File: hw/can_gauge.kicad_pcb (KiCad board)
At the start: 2 copper layers, 28 parts, among them J1 Gauge 1, J2 Gauge 2, J3 Gauge 3, J4 Gauge 4, J5 Gauge 5, J6 Gauge 6, J7 Power & CAN, U1 PIC16F1459-IP, U4 74HC595, U5 74HC595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

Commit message: hw: data traces
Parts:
- moved U1 6.29 mm to (88.9, 79.5)
- moved C9 4.00 mm to (86.0, 73.5)
- moved C4 3.93 mm to (90.0, 73.5), turned to -90 degrees
- moved U6 1.00 mm to (75.5, 73.8)
- moved C8 0.50 mm to (78.0, 95.0)
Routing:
- net Net-(U1-PWM1/CWG1A/T0CKI/RC5): track 26.2 -> 93.4 mm
- net +5V: track 75.7 -> 142.3 mm
- net Net-(U1-CWG1B/C1OUT/C2OUT/RC4): track 25.2 -> 77.0 mm
- net Net-(U4-QH'): track 0.00 -> 41.8 mm
- net Net-(U1-CLKR/C1IN3-/C2IN3-/DACOUT2/AN7/RC3): track 0.00 -> 35.9 mm
- net Net-(U5-QH'): track 39.6 -> 42.7 mm
- net Net-(U6-QG): track 14.3 -> 14.8 mm
- net GND: track 0.50 -> 0.00 mm, vias 20 -> 22

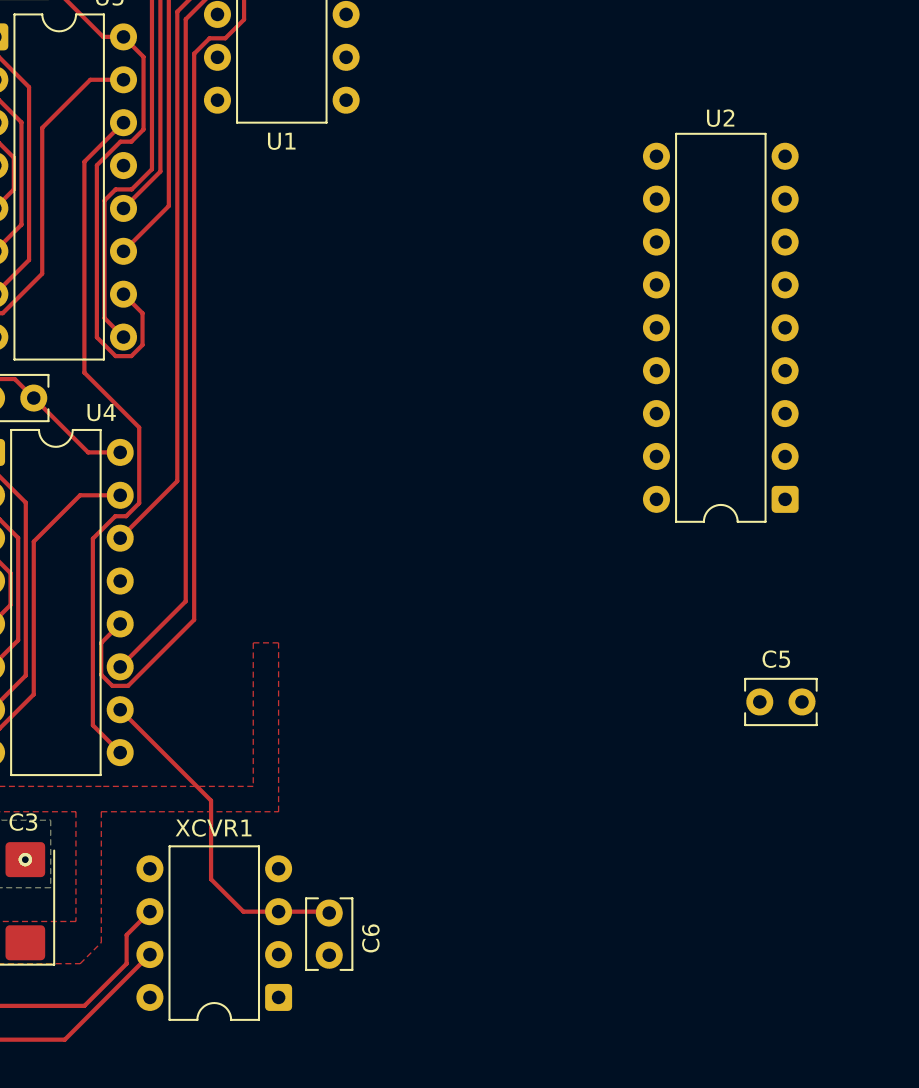
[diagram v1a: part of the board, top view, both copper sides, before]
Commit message: hw: rx,tx traces
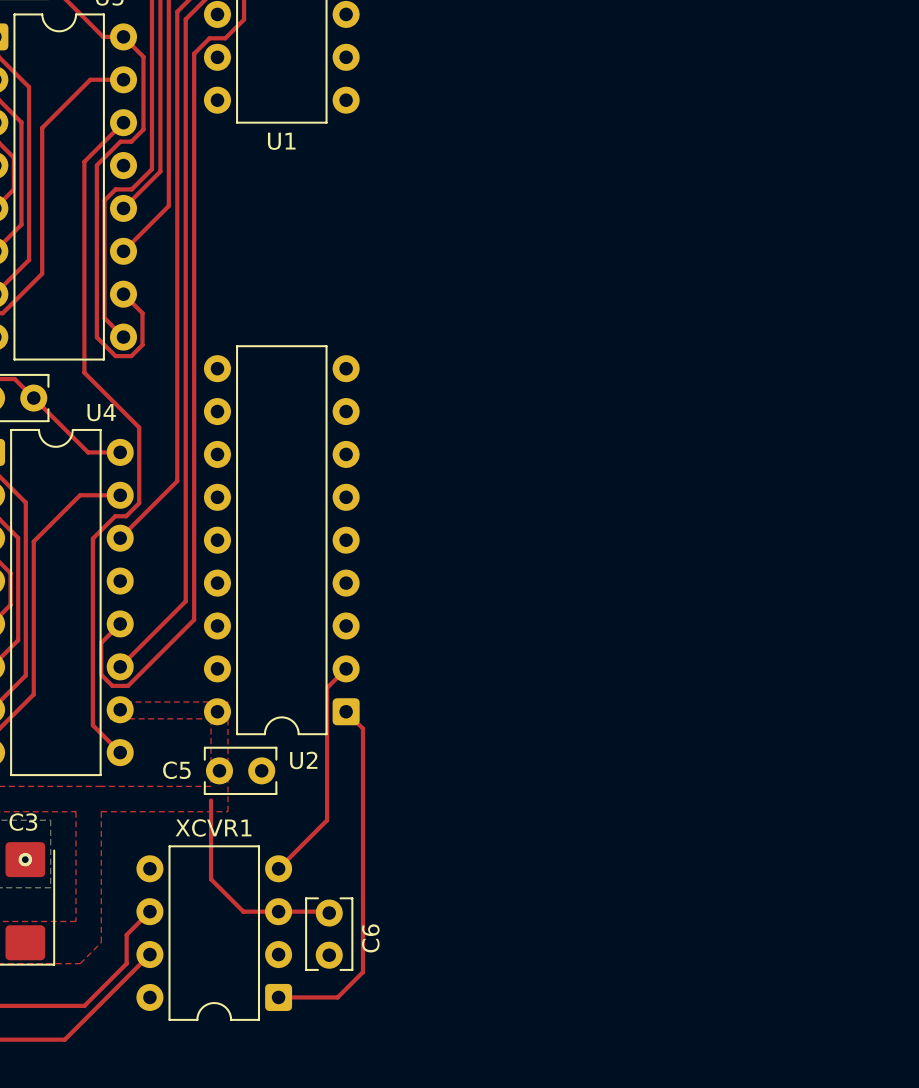
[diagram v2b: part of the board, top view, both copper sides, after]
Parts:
- moved C5 34.7 mm to (89.0, 142.1), turned to 0 degrees
- moved U2 28.9 mm to (96.5, 138.6)
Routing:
- net TX: track 0.27 -> 21.5 mm
- net RX: track 0.00 -> 13.5 mm
- net +5V: track 142.3 -> 134.7 mm
- net GND: vias 22 -> 23
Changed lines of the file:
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@@
 	(footprint "Capacitor_THT:C_Rect_L4.0mm_W2.5mm_P2.50mm"
 		(layer "F.Cu")
-		(at 123.5 138 180)
+		(at 89 142.08)
 		(descr "C, Rect series, Radial, pin pitch=2.50mm, , length*width=4*2.5mm^2, Capacitor")
 		(tags "C Rect series Radial pin pitch 2.50mm  length 4mm width 2.5mm Capacitor")
 		(property "Reference" "C5"
-			(at 1.5 2.5 0)
+			(at -2.5 0 0)
 			(layer "F.SilkS")
 			(effects
@@
 		)
 		(property "Datasheet" "https://product.tdk.com/en/system/files/dam/doc/product/capacitor/ceramic/lead-mlcc/catalog/leadmlcc_halogenfree_fa_en.pdf"
-			(at 0 0 180)
+			(at 0 0 0)
 			(unlocked yes)
 			(layer "F.Fab")
@@
 		)
 		(property "Description" "Unpolarized capacitor, small symbol"
-			(at 0 0 180)
+			(at 0 0 0)
 			(unlocked yes)
 			(layer "F.Fab")
@@
 		)
 		(property "Digikey" "https://www.digikey.ca/en/products/detail/tdk-corporation/FA18X7R1H104KNU06/5863626"
-			(at 0 0 180)
+			(at 0 0 0)
 			(unlocked yes)
 			(layer "F.Fab")
@@
 		(attr through_hole)
 		(fp_line
-			(start 3.37 0.665)
-			(end 3.37 1.37)
+			(start -0.87 -1.37)
+			(end -0.87 -0.665)
 			(stroke
 				(width 0.12)
@@
 		)
 		(fp_line
-			(start 3.37 -1.37)
-			(end 3.37 -0.665)
+			(start -0.87 -1.37)
+			(end 3.37 -1.37)
 			(stroke
 				(width 0.12)
@@
 		)
 		(fp_line
-			(start -0.87 1.37)
-			(end 3.37 1.37)
+			(start -0.87 0.665)
+			(end -0.87 1.37)
 			(stroke
 				(width 0.12)
@@
 		)
 		(fp_line
-			(start -0.87 0.665)
-			(end -0.87 1.37)
+			(start -0.87 1.37)
+			(end 3.37 1.37)
 			(stroke
 				(width 0.12)
@@
 		)
 		(fp_line
-			(start -0.87 -1.37)
-			(end 3.37 -1.37)
+			(start 3.37 -1.37)
+			(end 3.37 -0.665)
 			(stroke
 				(width 0.12)
@@
 		)
 		(fp_line
-			(start -0.87 -1.37)
-			(end -0.87 -0.665)
+			(start 3.37 0.665)
+			(end 3.37 1.37)
 			(stroke
 				(width 0.12)
@@
 		)
 		(fp_line
-			(start 3.55 1.5)
-			(end 3.55 -1.5)
+			(start -1.05 -1.5)
+			(end -1.05 1.5)
 			(stroke
 				(width 0.05)
@@
 		)
 		(fp_line
-			(start 3.55 -1.5)
-			(end -1.05 -1.5)
+			(start -1.05 1.5)
+			(end 3.55 1.5)
 			(stroke
 				(width 0.05)
@@
 		)
 		(fp_line
-			(start -1.05 1.5)
-			(end 3.55 1.5)
+			(start 3.55 -1.5)
+			(end -1.05 -1.5)
 			(stroke
 				(width 0.05)
@@
 		)
 		(fp_line
-			(start -1.05 -1.5)
-			(end -1.05 1.5)
+			(start 3.55 1.5)
+			(end 3.55 -1.5)
 			(stroke
 				(width 0.05)
@@
 		)
 		(fp_line
-			(start 3.25 1.25)
-			(end 3.25 -1.25)
+			(start -0.75 -1.25)
+			(end -0.75 1.25)
 			(stroke
 				(width 0.1)
@@
 		)
 		(fp_line
-			(start 3.25 -1.25)
-			(end -0.75 -1.25)
+			(start -0.75 1.25)
+			(end 3.25 1.25)
 			(stroke
 				(width 0.1)
@@
 		)
 		(fp_line
-			(start -0.75 1.25)
-			(end 3.25 1.25)
+			(start 3.25 -1.25)
+			(end -0.75 -1.25)
 			(stroke
 				(width 0.1)
@@
 		)
 		(fp_line
-			(start -0.75 -1.25)
-			(end -0.75 1.25)
+			(start 3.25 1.25)
+			(end 3.25 -1.25)
 			(stroke
 				(width 0.1)
@@
 		)
 		(pad "1" thru_hole circle
-			(at 0 0 180)
+			(at 0 0)
 			(size 1.6 1.6)
 			(drill 0.8)
@@
 		)
 		(pad "2" thru_hole circle
-			(at 2.5 0 180)
+			(at 2.5 0)
 			(size 1.6 1.6)
 			(drill 0.8)
@@
 	(footprint "Package_DIP:DIP-18_W7.62mm"
 		(layer "F.Cu")
-		(at 122.5 126 180)
+		(at 96.5 138.58 180)
 		(descr "18-lead though-hole mounted DIP package, row spacing 7.62mm (300 mils)")
 		(tags "THT DIP DIL PDIP 2.54mm 7.62mm 300mil")
 		(property "Reference" "U2"
-			(at 3.81 22.54 0)
+			(at 2.5 -2.92 0)
 			(layer "F.SilkS")
 			(effects
@@
 	)
 	(via
+		(at 91.5 142.08)
+		(size 0.8)
+		(drill 0.4)
+		(layers "F.Cu" "B.Cu")
+		(net 1)
+	)
+	(via
 		(at 71.62 120.8)
 		(size 0.8)
@@
 	)
 	(via
-		(at 122.5 105.68)
+		(at 96.5 118.26)
 		(size 0.8)
 		(drill 0.4)
@@
 	)
 	(segment
-		(start 83.12 138.46)
-		(end 88.5 143.84)
-		(width 0.25)
-		(layer "F.Cu")
-		(net 3)
-	)
-	(segment
 		(start 88 73.5)
 		(end 90 73.5)
@@
 	)
 	(segment
-		(start 122.31 125.69)
-		(end 122.5 125.5)
+		(start 95.374 145.006)
+		(end 95.374 137.166)
+		(width 0.25)
+		(layer "F.Cu")
+		(net 50)
+	)
+	(segment
+		(start 95.374 137.166)
+		(end 96.5 136.04)
+		(width 0.25)
+		(layer "F.Cu")
+		(net 50)
+	)
+	(segment
+		(start 92.5 147.88)
+		(end 95.374 145.006)
+		(width 0.25)
+		(layer "F.Cu")
+		(net 50)
+	)
+	(segment
+		(start 97.5 139.58)
+		(end 96.5 138.58)
+		(width 0.25)
+		(layer "F.Cu")
+		(net 53)
+	)
+	(segment
+		(start 96 155.5)
+		(end 97.5 154)
+		(width 0.25)
+		(layer "F.Cu")
+		(net 53)
+	)
+	(segment
+		(start 92.5 155.5)
+		(end 96 155.5)
+		(width 0.25)
+		(layer "F.Cu")
+		(net 53)
+	)
+	(segment
+		(start 97.5 154)
+		(end 97.5 139.58)
 		(width 0.25)
 		(layer "F.Cu")
@@
 			(pts
 				(xy 67.5 143) (xy 67.5 142.5) (xy 66 142.5) (xy 66 144.5) (xy 80.5 144.5) (xy 80.5 151) (xy 68.5 151)
-				(xy 68.5 153.5) (xy 80.75 153.5) (xy 82 152.25) (xy 82 144.5) (xy 92.5 144.5) (xy 92.5 134.5) (xy 91 134.5)
-				(xy 91 143) (xy 82 143)
+				(xy 68.5 153.5) (xy 80.75 153.5) (xy 82 152.25) (xy 82 144.5) (xy 89.5 144.5) (xy 89.5 138) (xy 82.5 138)
+				(xy 82.5 139) (xy 88.5 139) (xy 88.5 143) (xy 82 143)
 			)
 		)

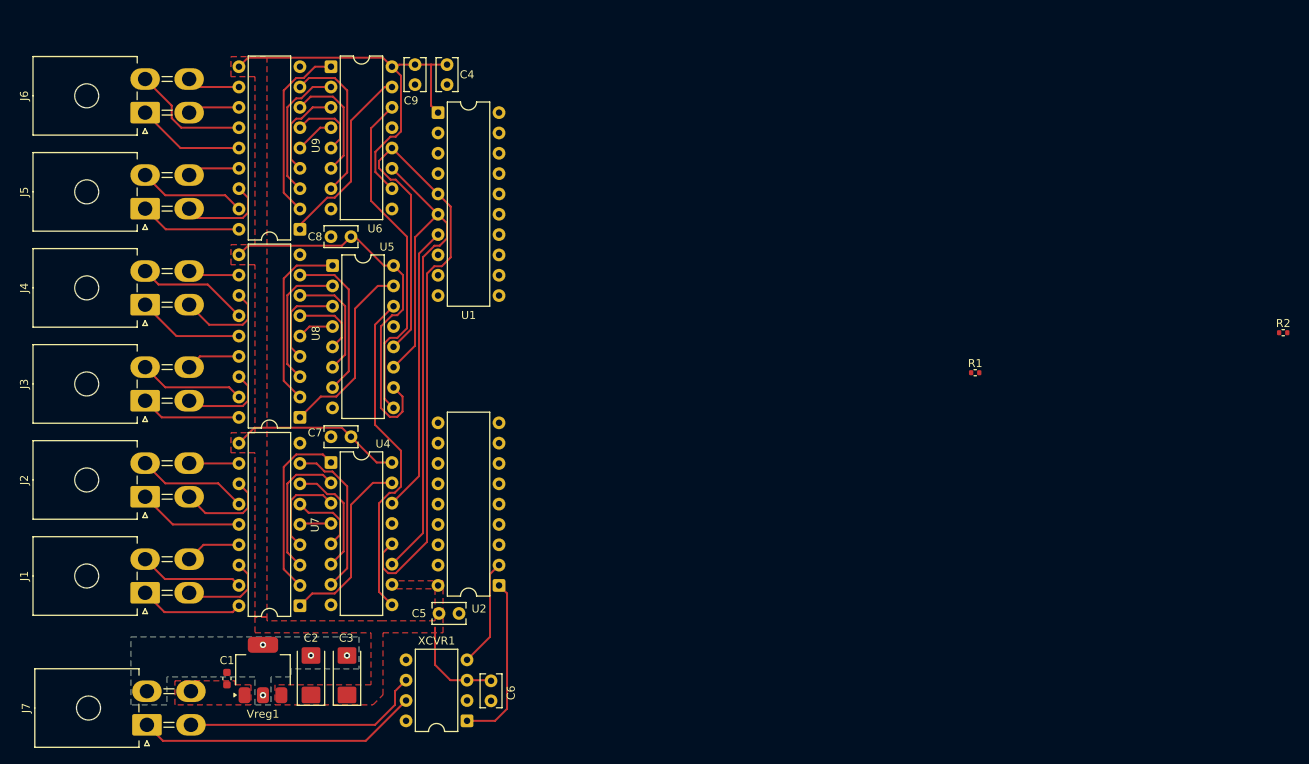
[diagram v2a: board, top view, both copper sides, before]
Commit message: hw: mcp2515 traces
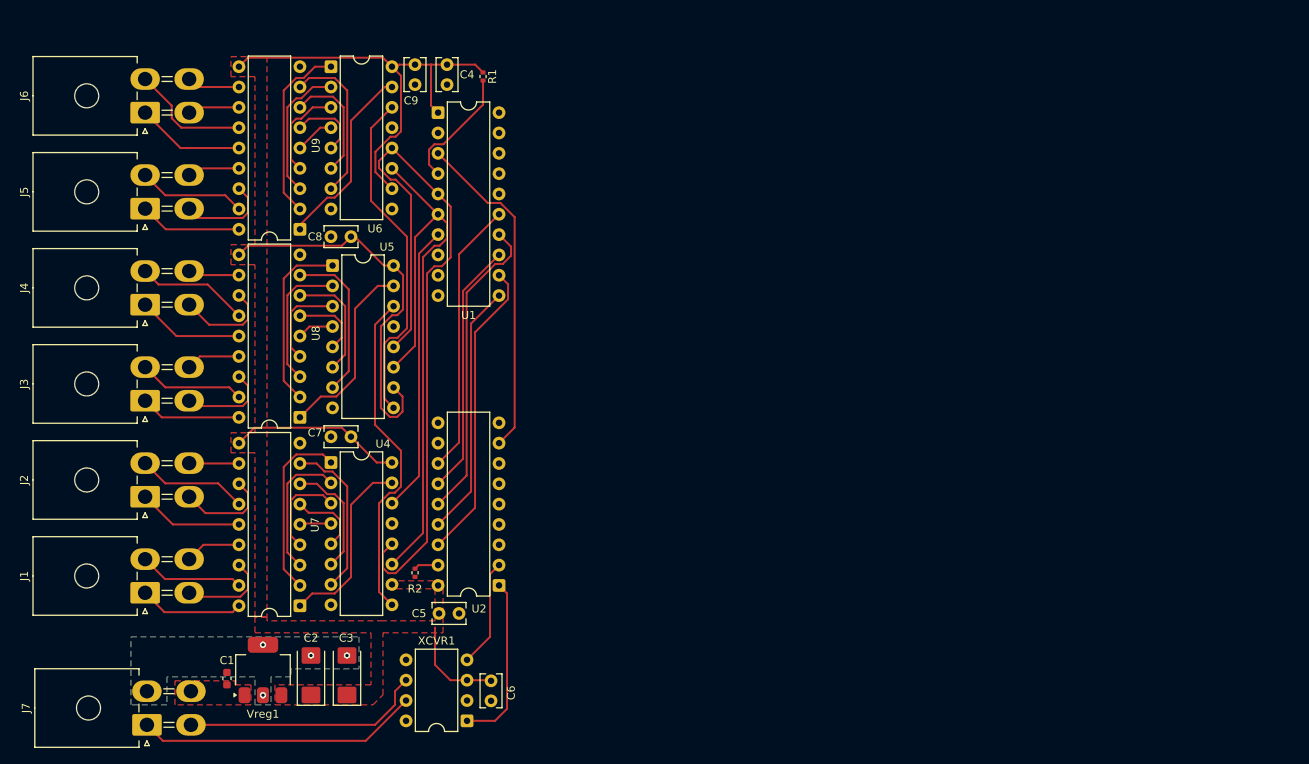
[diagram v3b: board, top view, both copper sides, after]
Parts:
- moved R2 112.6 mm to (86.0, 137.0), turned to -90 degrees
- moved R1 71.8 mm to (94.5, 75.0), turned to -90 degrees
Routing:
- net CLK: track 0.00 -> 41.9 mm
- net SO: track 0.00 -> 38.6 mm
- net ~{CS}: track 0.00 -> 37.8 mm
- net ~{INT}: track 0.00 -> 34.3 mm
- net SI: track 0.00 -> 31.8 mm
- net SCK: track 0.00 -> 31.8 mm
- net Net-(U1-RA3/T1G/~{SS}/~{MCLR}/Vpp): track 0.00 -> 15.5 mm
- net +5V: track 134.7 -> 139.6 mm
- net Net-(U2-~{RESET}): track 0.00 -> 3.06 mm

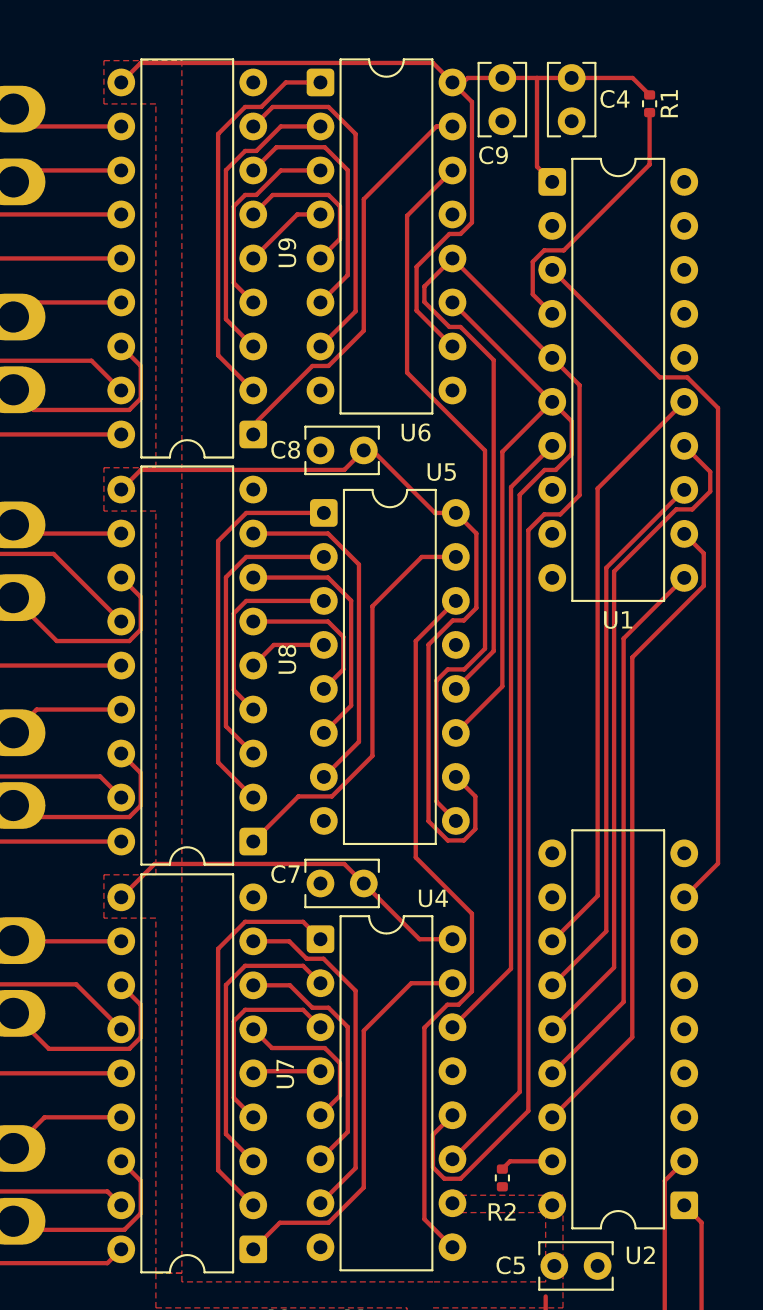
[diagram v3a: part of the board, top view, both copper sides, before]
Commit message: hw: extend power plane
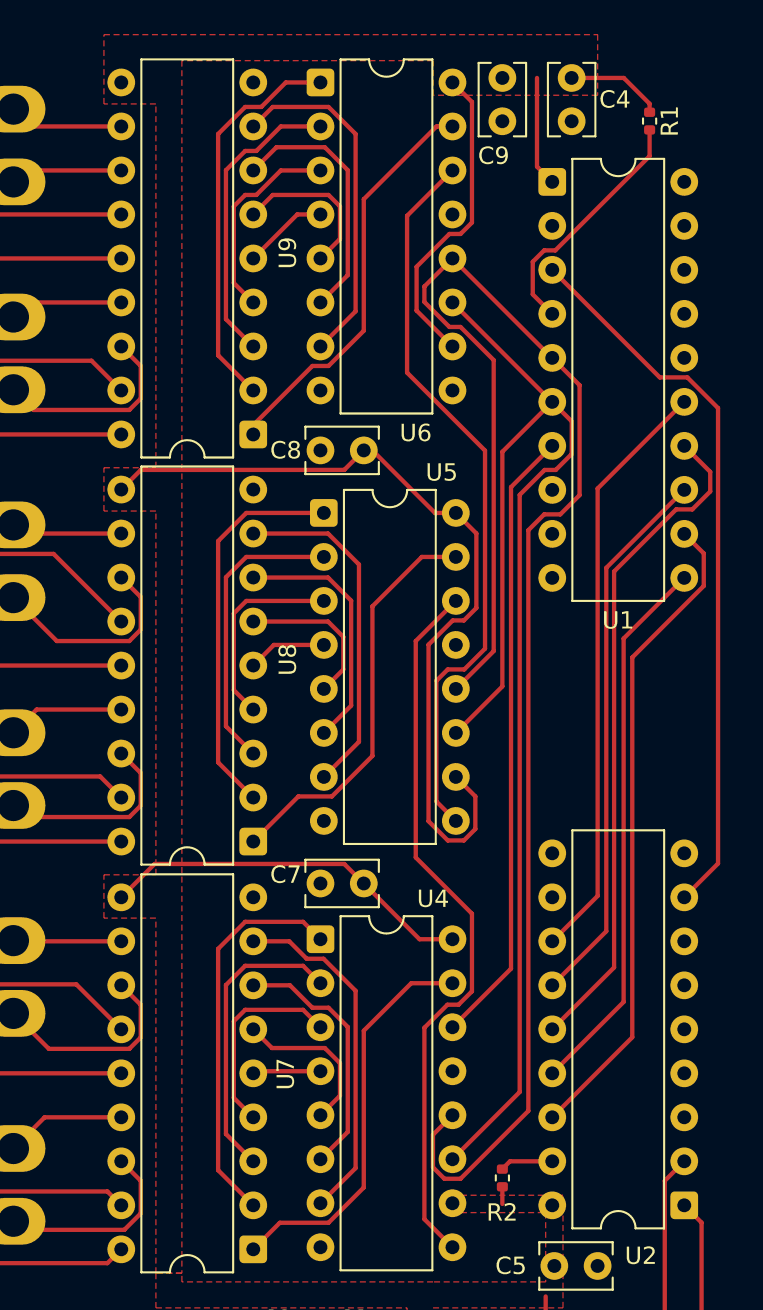
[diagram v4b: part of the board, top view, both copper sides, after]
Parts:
- moved R1 1.00 mm to (94.5, 76.0)
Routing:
- net +5V: track 139.6 -> 114.3 mm
- net Net-(U1-RA3/T1G/~{SS}/~{MCLR}/Vpp): track 15.5 -> 14.3 mm
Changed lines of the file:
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@@
 	(footprint "Resistor_SMD:R_0402_1005Metric"
 		(layer "F.Cu")
-		(at 94.5 74.99 -90)
+		(at 94.5 75.99 -90)
 		(descr "Resistor SMD 0402 (1005 Metric), square (rectangular) end terminal, IPC_7351 nominal, (Body size source: IPC-SM-782 page 72, https://www.pcb-3d.com/wordpress/wp-content/uploads/ipc-sm-782a_amendment_1_and_2.pdf), generated with kicad-footprint-generator")
 		(tags "resistor")
@@
 	)
 	(segment
-		(start 65.126 72.634)
-		(end 64 73.76)
+		(start 86 137.51)
+		(end 86 138.5)
 		(width 0.25)
 		(layer "F.Cu")
@@
 	)
 	(segment
-		(start 84.246 74.886)
-		(end 83.12 73.76)
+		(start 94.5 74.99)
+		(end 94.5 75.48)
 		(width 0.25)
 		(layer "F.Cu")
@@
 	)
 	(segment
-		(start 94.5 74.48)
-		(end 93.52 73.5)
+		(start 84.246 74.886)
+		(end 83.12 73.76)
 		(width 0.25)
 		(layer "F.Cu")
@@
 	)
 	(segment
-		(start 93.52 73.5)
-		(end 90 73.5)
-		(width 0.25)
-		(layer "F.Cu")
-		(net 3)
-	)
-	(segment
 		(start 90.42 150.42)
 		(end 92.5 150.42)
@@
 	)
 	(segment
-		(start 84 73.5)
-		(end 86 73.5)
-		(width 0.25)
-		(layer "F.Cu")
-		(net 3)
-	)
-	(segment
 		(start 83.315 113.85)
 		(end 84.441 114.976)
@@
 	)
 	(segment
-		(start 83.12 73.76)
-		(end 81.994 72.634)
-		(width 0.25)
-		(layer "F.Cu")
-		(net 3)
-	)
-	(segment
 		(start 81.049 86.929)
 		(end 81.049 84.398595)
@@
 	)
 	(segment
-		(start 86 73.5)
-		(end 88 73.5)
-		(width 0.25)
-		(layer "F.Cu")
-		(net 3)
-	)
-	(segment
-		(start 83.74 73.76)
-		(end 84 73.5)
+		(start 93.01 73.5)
+		(end 94.5 74.99)
 		(width 0.25)
 		(layer "F.Cu")
@@
 	)
 	(segment
-		(start 81.994 72.634)
-		(end 65.126 72.634)
-		(width 0.25)
-		(layer "F.Cu")
-		(net 3)
-	)
-	(segment
-		(start 88 73.5)
-		(end 90 73.5)
+		(start 90 73.5)
+		(end 93.01 73.5)
 		(width 0.25)
 		(layer "F.Cu")
@@
 	)
 	(segment
-		(start 83.12 73.76)
-		(end 83.74 73.76)
-		(width 0.25)
-		(layer "F.Cu")
-		(net 3)
-	)
-	(segment
 		(start 83.586405 82.506)
 		(end 84.246 81.846405)
@@
 	)
 	(segment
-		(start 94.5 78.5)
-		(end 94.5 75.5)
+		(start 88.413595 83.454)
+		(end 89.058405 83.454)
 		(width 0.25)
 		(layer "F.Cu")
@@
 	)
 	(segment
-		(start 88.88 87.12)
-		(end 87.754 85.994)
+		(start 94.5 78.012405)
+		(end 94.5 76.5)
 		(width 0.25)
 		(layer "F.Cu")
@@
 	)
 	(segment
-		(start 87.754 85.994)
-		(end 87.754 84.113595)
+		(start 87.754 84.113595)
+		(end 88.413595 83.454)
 		(width 0.25)
 		(layer "F.Cu")
@@
 	)
 	(segment
-		(start 87.754 84.113595)
-		(end 88.413595 83.454)
+		(start 89.058405 83.454)
+		(end 94.5 78.012405)
 		(width 0.25)
 		(layer "F.Cu")
@@
 	)
 	(segment
-		(start 89.546 83.454)
-		(end 94.5 78.5)
+		(start 88.88 87.12)
+		(end 87.754 85.994)
 		(width 0.25)
 		(layer "F.Cu")
@@
 	)
 	(segment
-		(start 88.413595 83.454)
-		(end 89.546 83.454)
+		(start 87.754 85.994)
+		(end 87.754 84.113595)
 		(width 0.25)
 		(layer "F.Cu")
@@
 		(polygon
 			(pts
-				(xy 67.5 72.5) (xy 67.5 142.5) (xy 66 142.5) (xy 66 122) (xy 63 122) (xy 63 119.5) (xy 66 119.5)
-				(xy 66 98.5) (xy 63 98.5) (xy 63 96) (xy 66 96) (xy 66 75) (xy 63 75) (xy 63 72.5)
+				(xy 63 71) (xy 91.5 71) (xy 91.5 74.5) (xy 82 74.5) (xy 82 72.5) (xy 67.5 72.5) (xy 67.5 142.5)
+				(xy 66 142.5) (xy 66 122) (xy 63 122) (xy 63 119.5) (xy 66 119.5) (xy 66 98.5) (xy 63 98.5) (xy 63 96)
+				(xy 66 96) (xy 66 75) (xy 63 75)
 			)
 		)
